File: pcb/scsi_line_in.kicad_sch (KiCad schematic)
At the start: 0 parts

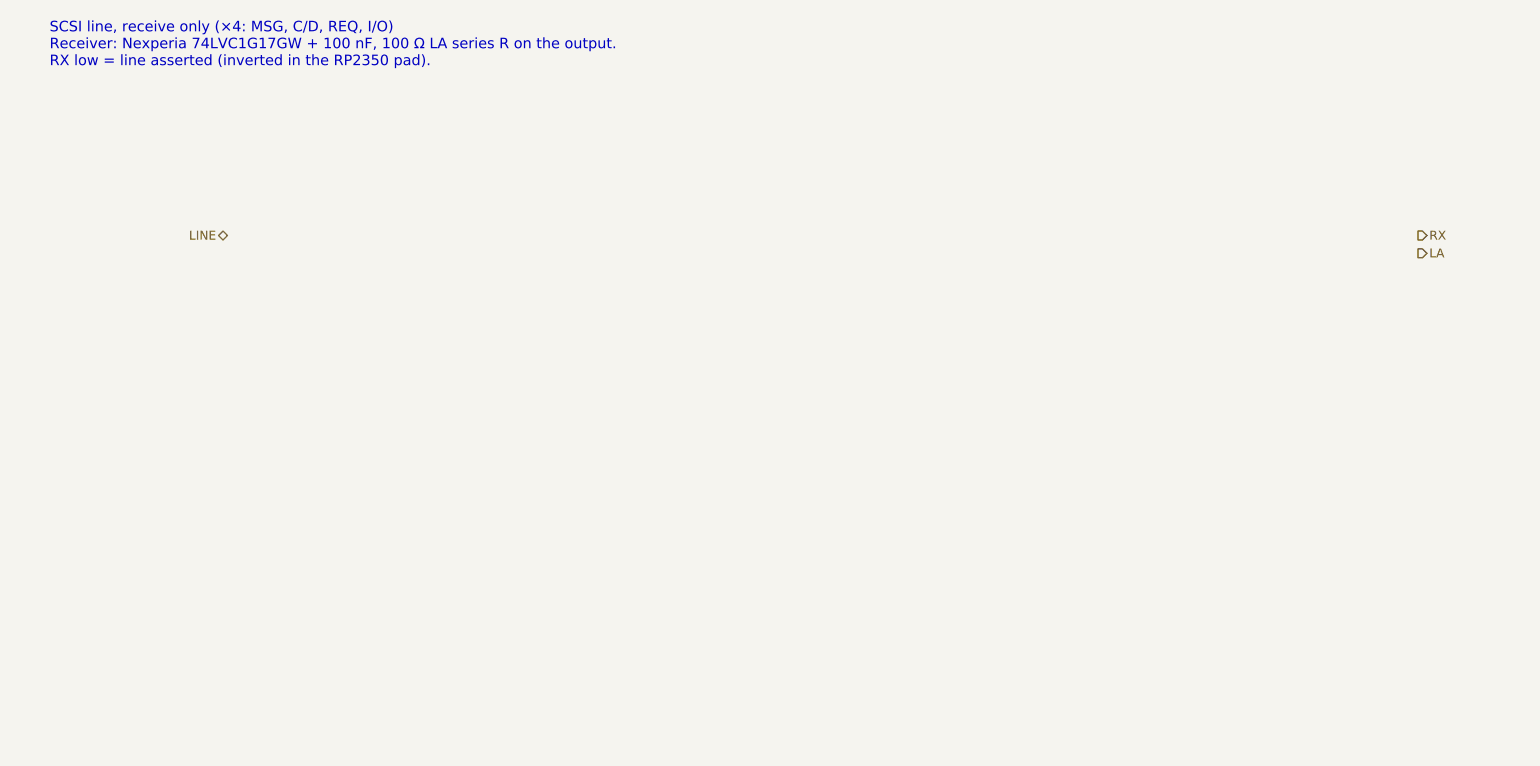
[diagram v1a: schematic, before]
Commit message: Phase 3: populate SCSI sheet and channel sheets
SCSI sheet (A2): IDC50 and HD50 wired by signal name from SCSI-2
Table 2, all four RESERVED lines grounded through 0R links, the
logic-analyzer header as a pin-for-pin copy of the Digital Discovery
DIN connector, three SN74LVTH245A terminators with their DIP-switch
enable and truth table, and one cluster per line: 2 x 220R terminator
pair, ESD diode and channel sheet. Channel sheets hold the FDV301N
driver and the 74LVC1G17 receiver; 18 instances, references page x 100.

Generator: repeated sheets, sheet symbols, native tables, and
deterministic UUIDs. Nets renamed: LA -> LOGIC_ANALYZER,
TERMINATOR_EN -> TERMINATOR_EN_INVERTED_FIRMWARE.
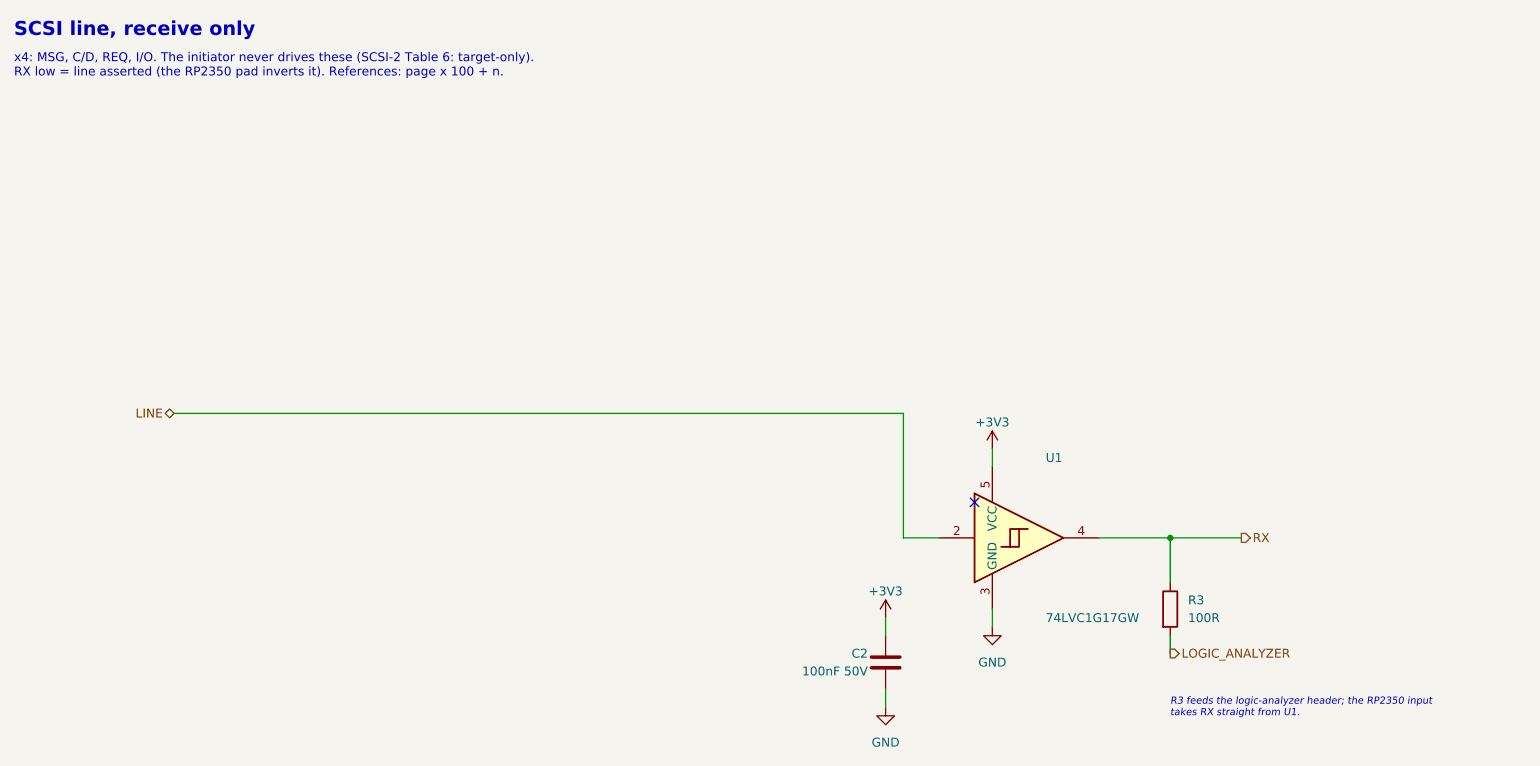
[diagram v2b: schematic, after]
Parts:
- added C2: 100nF 50V, Capacitor_SMD:C_0402_1005Metric, symbol Device:C
- added R3: 100R, Resistor_SMD:R_0402_1005Metric, symbol Device:R
- added U1: 74LVC1G17GW, Package_TO_SOT_SMD:SOT-353_SC-70-5, symbol 74xGxx:74LVC1G17
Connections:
- net LINE: now also U1.2
- net RX: now also R3.1, U1.4
- new net +3V3: C2.1, U1.5 (VCC)
- new net GND: C2.2, U1.3 (GND)
- new net LOGIC_ANALYZER: R3.2
- no-connect marks 0 -> 1
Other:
- note added: "R3 feeds the logic-analyzer header; the RP2350 input takes RX straight from U1."
- note added: "SCSI line, receive only"
- note added: "x4: MSG, C/D, REQ, I/O. The initiator never drives these (SCSI-2 Table 6: target-only). RX low = line asserted (the RP2350 pad inverts it). References: page x 100 + n."
- note removed: "SCSI line, receive only (×4: MSG, C/D, REQ, I/O) Receiver: Nexperia 74LVC1G17GW + 100 nF, 100 Ω LA series R on the output. RX low = line asserted (inverted in the RP2350 pad)."

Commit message: route more scsi traces
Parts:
- renumbered C2 to C2202, R3 to R2203, U1 to U2201
